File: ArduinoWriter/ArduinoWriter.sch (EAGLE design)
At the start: 27 parts, among them IC1 ATMEGA328-PU, IC2 TC74HC08AP, IC3 TC74HC32AP, Q1 HUSG-16.000-20, U1 ARRDUINOUNO-NOSILK

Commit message: レイアウト完了
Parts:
- added 5V_OUT: OSBL1608C1A, LED:OSBL1608C1A
- added C3, C4: 10u, RCL:C2012
- added R10, R11, R12: 1k, RCL:R1608
- added RX_LED, TX_LED: OSTG1608C1A, LED:OSTG1608C1A
- added T1, T2: IRLML6344TRPBF, FET:IRLML6344TRPBF
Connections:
- new net N$10: 5V_OUT.A, R10.1
- new net N$11: RX_LED.C, T1.D
- new net N$12: T2.D, TX_LED.C
- new net N$13: R11.1, RX_LED.A
- new net N$14: R12.1, TX_LED.A
- new net SE_SW_LED: IC3C.O, R7.2
- new net WR_SW_LED: IC3D.O, R6.2
- net +5V: now also C3.1, C4.1, IC2P.VCC, IC3P.VCC, R11.2, R12.2
- net GND: now also 5V_OUT.C, C3.2, C4.2, IC2P.GND, IC3C.I1, IC3D.I1, IC3P.GND, T1.S, T2.S
- net PCRX_ICTX: now also T1.G
- net PCTX_ICRX: now also T2.G
- net PROG_SUPPLY: now also R10.2
- net SE_SW: now also IC3C.I0; no longer R7.2
- net WR_SW: now also IC3D.I0; no longer R6.2
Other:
- moved on the sheet: 3.3V, 5V, C1, C2, ERR, HB, IC1, IC2A, IC2B, IC2C, IC2D, IC2P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

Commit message: 配線・シルク完
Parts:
- added POWER: (no value), pinhead:PINHD-1X3
- added RESET: TS-06104, タクトスイッチ:TS-06104
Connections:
- net +3.3V: now also POWER.2
- net +5V: now also POWER.1
- net GND: now also POWER.3, RESET.T3, RESET.T4
- net RESET_SIG: now also RESET.T1, RESET.T2
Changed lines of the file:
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@@
 <part name="SUPPLY28" library="supply" deviceset="GND" device=""/>
 <part name="SUPPLY29" library="supply2" library_urn="urn:adsk.eagle:library:372" deviceset="GND" device=""/>
+<part name="RESET" library="タクトスイッチ" deviceset="TS-06104" device="" package3d_urn="urn:adsk.eagle:package:29147268/2"/>
+<part name="SUPPLY30" library="supply" deviceset="GND" device=""/>
+<part name="POWER" library="pinhead" deviceset="PINHD-1X3" device="" package3d_urn="urn:adsk.eagle:package:22458/2"/>
+<part name="SUPPLY31" library="supply" deviceset="+5V" device=""/>
+<part name="U$4" library="supply" deviceset="+3.3V" device=""/>
+<part name="SUPPLY32" library="MyParts" deviceset="GND" device=""/>
 </parts>
 <sheets>
@@
 <attribute name="VALUE" x="151.765" y="155.575" size="1.778" layer="96"/>
 </instance>
+<instance part="RESET" gate="G$1" x="189.23" y="76.2" smashed="yes">
+<attribute name="NAME" x="185.42" y="69.85" size="1.27" layer="95"/>
+<attribute name="VALUE" x="185.42" y="67.31" size="1.27" layer="96"/>
+</instance>
+<instance part="SUPPLY30" gate="GND" x="181.61" y="66.04" smashed="yes">
+<attribute name="VALUE" x="179.705" y="62.865" size="1.778" layer="96"/>
+</instance>
+<instance part="POWER" gate="A" x="193.04" y="121.92" smashed="yes">
+<attribute name="NAME" x="186.69" y="127.635" size="1.778" layer="95"/>
+<attribute name="VALUE" x="186.69" y="114.3" size="1.778" layer="96"/>
+</instance>
+<instance part="SUPPLY31" gate="+5V" x="185.42" y="132.08" smashed="yes">
+<attribute name="VALUE" x="183.515" y="135.255" size="1.778" layer="96"/>
+</instance>
+<instance part="U$4" gate="G$1" x="181.61" y="135.89" smashed="yes">
+<attribute name="VALUE" x="179.705" y="139.065" size="1.778" layer="96"/>
+</instance>
+<instance part="SUPPLY32" gate="GND" x="185.42" y="111.76" smashed="yes"/>
 </instances>
 <busses>
@@
 <junction x="153.67" y="165.1"/>
 </segment>
+<segment>
+<pinref part="SUPPLY30" gate="GND" pin="GND"/>
+<pinref part="RESET" gate="G$1" pin="T3"/>
+<wire x1="181.61" y1="68.58" x2="181.61" y2="73.66" width="0.1524" layer="91"/>
+<pinref part="RESET" gate="G$1" pin="T4"/>
+<wire x1="196.85" y1="73.66" x2="181.61" y2="73.66" width="0.1524" layer="91"/>
+<junction x="181.61" y="73.66"/>
+</segment>
+<segment>
+<pinref part="POWER" gate="A" pin="3"/>
+<wire x1="190.5" y1="119.38" x2="185.42" y2="119.38" width="0.1524" layer="91"/>
+<wire x1="185.42" y1="119.38" x2="185.42" y2="114.3" width="0.1524" layer="91"/>
+<pinref part="SUPPLY32" gate="GND" pin="GND"/>
+</segment>
 </net>
 <net name="+5V" class="0">
@@
 <junction x="160.02" y="83.82"/>
 </segment>
+<segment>
+<pinref part="SUPPLY31" gate="+5V" pin="+5V"/>
+<pinref part="POWER" gate="A" pin="1"/>
+<wire x1="185.42" y1="129.54" x2="185.42" y2="124.46" width="0.1524" layer="91"/>
+<wire x1="185.42" y1="124.46" x2="190.5" y2="124.46" width="0.1524" layer="91"/>
+</segment>
 </net>
 <net name="+3.3V" class="0">
@@
 <pinref part="R9" gate="G$1" pin="2"/>
 <pinref part="U$3" gate="G$1" pin="+3.3V"/>
+</segment>
+<segment>
+<pinref part="U$4" gate="G$1" pin="+3.3V"/>
+<pinref part="POWER" gate="A" pin="2"/>
+<wire x1="181.61" y1="133.35" x2="181.61" y2="121.92" width="0.1524" layer="91"/>
+<wire x1="181.61" y1="121.92" x2="190.5" y2="121.92" width="0.1524" layer="91"/>
 </segment>
 </net>
@@
 <label x="139.7" y="261.62" size="1.778" layer="95"/>
 </segment>
-</net>
+<segment>
+<pinref part="RESET" gate="G$1" pin="T1"/>
+<wire x1="181.61" y1="78.74" x2="181.61" y2="83.82" width="0.1524" layer="91"/>
+<wire x1="181.61" y1="83.82" x2="196.85" y2="83.82" width="0.1524" layer="91"/>
+<label x="182.88" y="83.82" size="1.778" layer="95"/>
+<pinref part="RESET" gate="G$1" pin="T2"/>
+<wire x1="181.61" y1="78.74" x2="195.58" y2="78.74" width="0.1524" layer="91"/>
+<junction x="181.61" y="78.74"/>
+<wire x1="196.85" y1="78.74" x2="195.58" y2="78.74" width="0.1524" layer="91"/>
+</segment>
+</net>

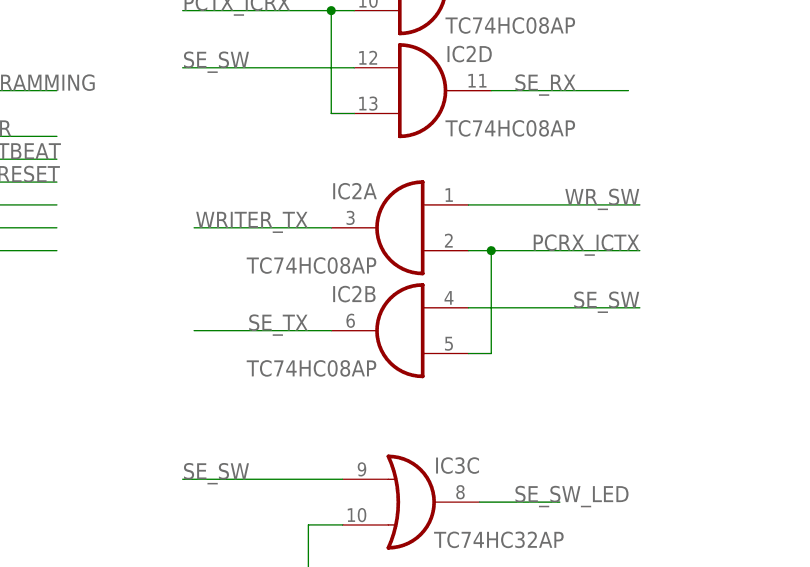
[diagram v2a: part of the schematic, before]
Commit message: RXTX欠陥部修正
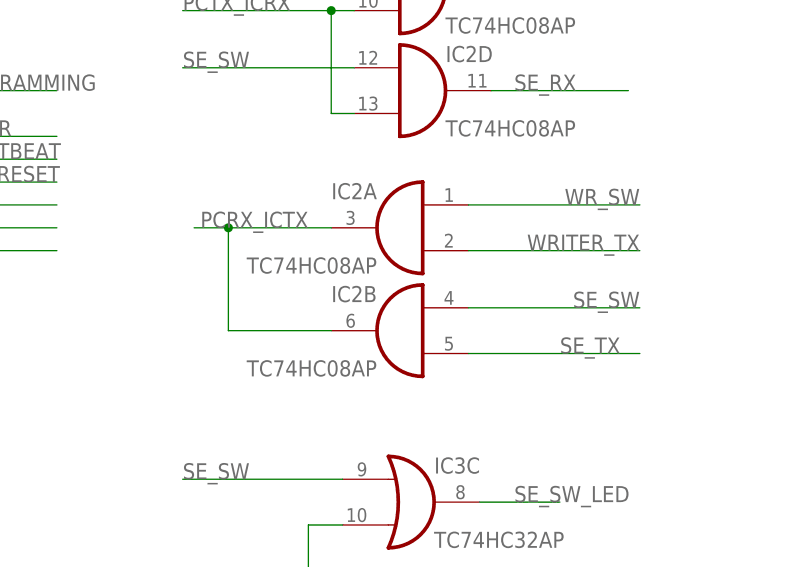
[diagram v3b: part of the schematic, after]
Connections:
- net PCRX_ICTX: now also IC2A.O, IC2B.O; no longer IC2A.I1, IC2B.I1
- net SE_TX: now also IC2B.I1; no longer IC2B.O
- net WRITER_TX: now also IC2A.I1; no longer IC2A.O
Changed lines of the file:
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@@
 <net name="PCRX_ICTX" class="0">
-<segment>
-<pinref part="IC2" gate="B" pin="I1"/>
-<wire x1="171.45" y1="196.85" x2="173.99" y2="196.85" width="0.1524" layer="91"/>
-<wire x1="173.99" y1="196.85" x2="173.99" y2="208.28" width="0.1524" layer="91"/>
-<pinref part="IC2" gate="A" pin="I1"/>
-<wire x1="173.99" y1="208.28" x2="171.45" y2="208.28" width="0.1524" layer="91"/>
-<wire x1="190.5" y1="208.28" x2="173.99" y2="208.28" width="0.1524" layer="91"/>
-<junction x="173.99" y="208.28"/>
-<label x="190.5" y="208.28" size="1.778" layer="95" rot="MR0"/>
-</segment>
 <segment>
 <pinref part="U1" gate="G$1" pin="1"/>
@@
 <label x="57.15" y="62.23" size="1.778" layer="95" rot="R90"/>
 </segment>
+<segment>
+<pinref part="IC2" gate="A" pin="O"/>
+<wire x1="156.21" y1="210.82" x2="144.78" y2="210.82" width="0.1524" layer="91"/>
+<label x="153.67" y="210.82" size="1.778" layer="95" rot="MR0"/>
+<pinref part="IC2" gate="B" pin="O"/>
+<wire x1="144.78" y1="210.82" x2="140.97" y2="210.82" width="0.1524" layer="91"/>
+<wire x1="156.21" y1="199.39" x2="144.78" y2="199.39" width="0.1524" layer="91"/>
+<wire x1="144.78" y1="199.39" x2="144.78" y2="210.82" width="0.1524" layer="91"/>
+<junction x="144.78" y="210.82"/>
+</segment>
 </net>
 <net name="WRITER_TX" class="0">
-<segment>
-<pinref part="IC2" gate="A" pin="O"/>
-<wire x1="156.21" y1="210.82" x2="140.97" y2="210.82" width="0.1524" layer="91"/>
-<label x="153.67" y="210.82" size="1.778" layer="95" rot="MR0"/>
-</segment>
 <segment>
 <pinref part="IC1" gate="1" pin="DIGITAL_1(TX)"/>
@@
 <label x="111.76" y="241.3" size="1.778" layer="95"/>
 </segment>
+<segment>
+<pinref part="IC2" gate="A" pin="I1"/>
+<wire x1="190.5" y1="208.28" x2="171.45" y2="208.28" width="0.1524" layer="91"/>
+<label x="190.5" y="208.28" size="1.778" layer="95" rot="MR0"/>
+</segment>
 </net>
 <net name="SE_TX" class="0">
-<segment>
-<pinref part="IC2" gate="B" pin="O"/>
-<wire x1="156.21" y1="199.39" x2="140.97" y2="199.39" width="0.1524" layer="91"/>
-<label x="153.67" y="199.39" size="1.778" layer="95" rot="MR0"/>
-</segment>
 <segment>
 <pinref part="SEPR" gate="A" pin="3"/>
@@
 <label x="134.62" y="127" size="1.778" layer="95"/>
 </segment>
+<segment>
+<pinref part="IC2" gate="B" pin="I1"/>
+<wire x1="171.45" y1="196.85" x2="190.5" y2="196.85" width="0.1524" layer="91"/>
+<label x="181.61" y="196.85" size="1.778" layer="95"/>
+</segment>
 </net>

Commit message: スイッチ・一部表示変更
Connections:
- net PROG_SUPPLY: now also SEPR.4
- net SE_RX: now also SEPR.3; no longer SEPR.1
- net SE_TX: now also SEPR.1; no longer SEPR.3
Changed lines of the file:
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@@
 </segment>
 <segment>
-<pinref part="SEPR" gate="A" pin="1"/>
-<wire x1="156.21" y1="129.54" x2="134.62" y2="129.54" width="0.1524" layer="91"/>
-<label x="134.62" y="129.54" size="1.778" layer="95"/>
+<pinref part="SEPR" gate="A" pin="3"/>
+<wire x1="156.21" y1="127" x2="134.62" y2="127" width="0.1524" layer="91"/>
+<label x="134.62" y="127" size="1.778" layer="95"/>
 </segment>
 </net>
@@
 <net name="SE_TX" class="0">
 <segment>
-<pinref part="SEPR" gate="A" pin="3"/>
-<wire x1="156.21" y1="127" x2="134.62" y2="127" width="0.1524" layer="91"/>
-<label x="134.62" y="127" size="1.778" layer="95"/>
-</segment>
-<segment>
 <pinref part="IC2" gate="B" pin="I1"/>
 <wire x1="171.45" y1="196.85" x2="190.5" y2="196.85" width="0.1524" layer="91"/>
 <label x="181.61" y="196.85" size="1.778" layer="95"/>
+</segment>
+<segment>
+<pinref part="SEPR" gate="A" pin="1"/>
+<wire x1="156.21" y1="129.54" x2="134.62" y2="129.54" width="0.1524" layer="91"/>
+<label x="134.62" y="129.54" size="1.778" layer="95"/>
 </segment>
 </net>
@@
 <pinref part="ICSP" gate="A" pin="2"/>
 <wire x1="163.83" y1="111.76" x2="172.72" y2="111.76" width="0.1524" layer="91"/>
-<wire x1="172.72" y1="111.76" x2="172.72" y2="129.54" width="0.1524" layer="91"/>
+<wire x1="172.72" y1="111.76" x2="172.72" y2="127" width="0.1524" layer="91"/>
 <pinref part="SEPR" gate="A" pin="2"/>
+<wire x1="172.72" y1="127" x2="172.72" y2="129.54" width="0.1524" layer="91"/>
 <wire x1="172.72" y1="129.54" x2="172.72" y2="138.43" width="0.1524" layer="91"/>
 <wire x1="163.83" y1="129.54" x2="172.72" y2="129.54" width="0.1524" layer="91"/>
@@
 <wire x1="172.72" y1="138.43" x2="154.94" y2="138.43" width="0.1524" layer="91"/>
 <label x="154.94" y="138.43" size="1.778" layer="95"/>
+<pinref part="SEPR" gate="A" pin="4"/>
+<wire x1="163.83" y1="127" x2="172.72" y2="127" width="0.1524" layer="91"/>
+<junction x="172.72" y="127"/>
 </segment>
 <segment>
